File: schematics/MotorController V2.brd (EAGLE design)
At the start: 120.6 x 100 mm, 52 parts, among them IC1 7805, Q1 BC307

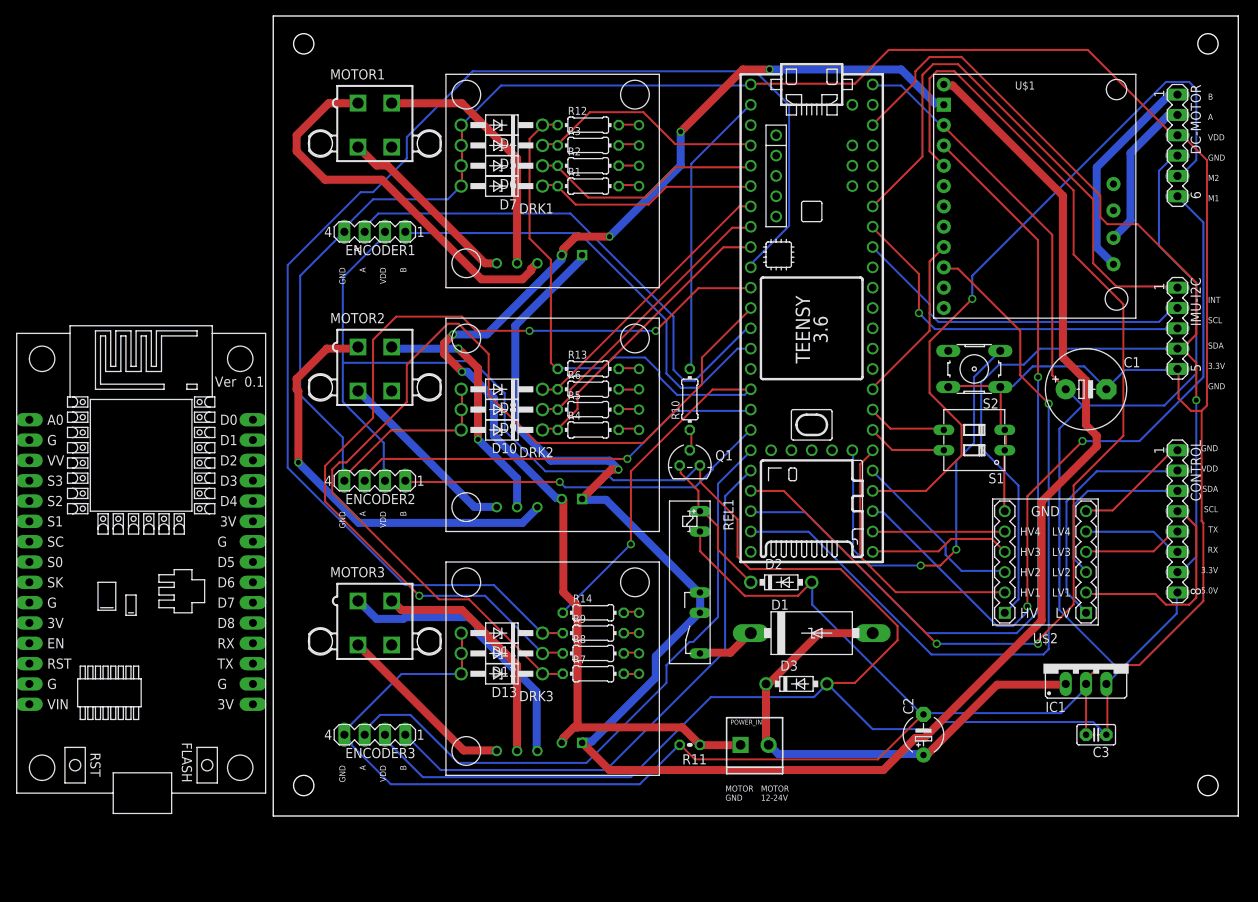
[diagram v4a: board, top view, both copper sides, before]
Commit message: i2c between webserver and bot controller
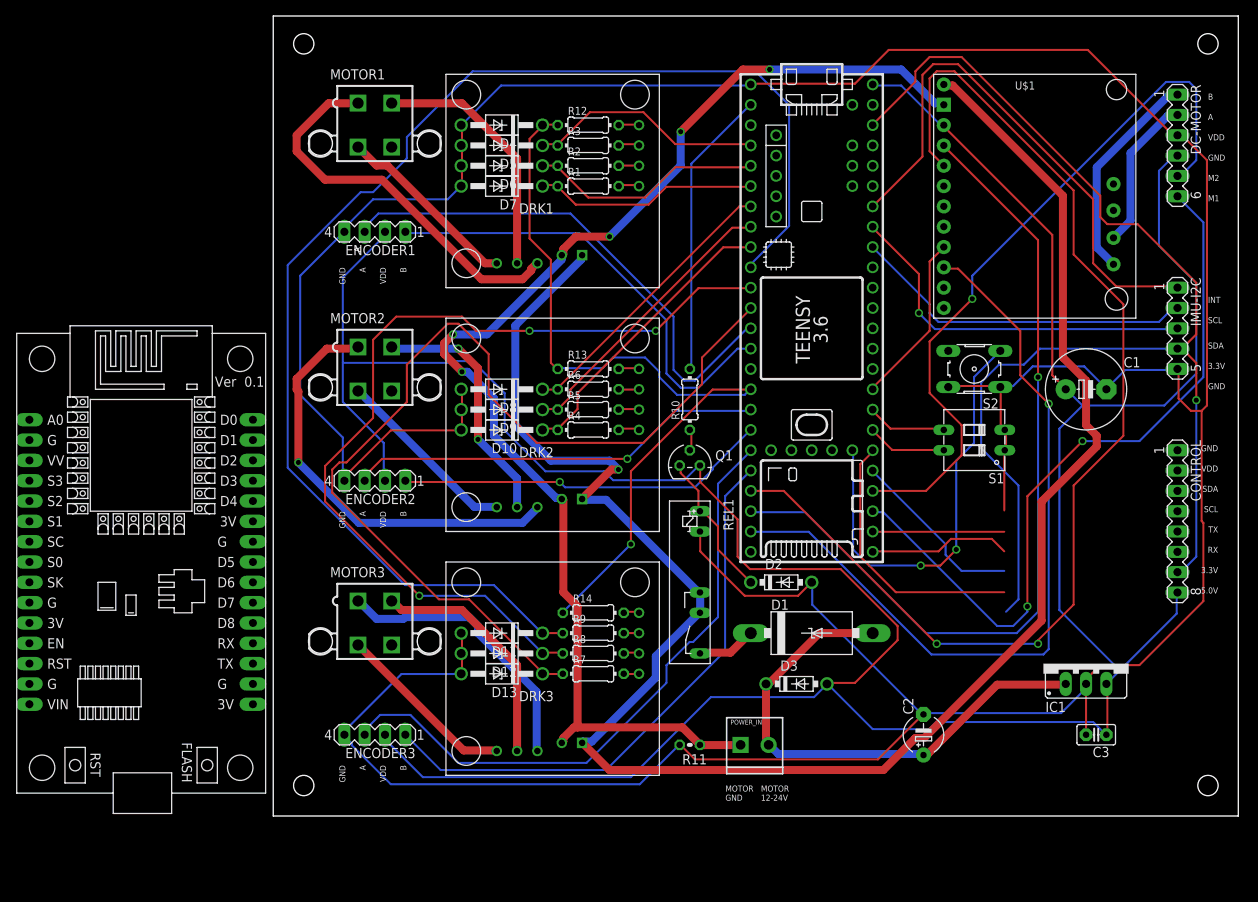
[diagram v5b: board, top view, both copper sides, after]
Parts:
- removed U$2: LEVEL-SHIFTER-4CHLEVEL-SHIFTER-4CH-ADAFRUIT, diy-modules:LEVEL-SHIFTER-4CH-ADAFRUIT
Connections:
- removed net CTR-SCL: CONTROL.4, U$2.LV1
- removed net CTR-SDA: CONTROL.3, U$2.LV2
- removed net CTRL-GND: CONTROL.1, U$2.GNDL
- removed net CTRL-RX: CONTROL.6, U$2.LV4
- removed net CTRL-TX: CONTROL.5, U$2.LV3
- removed net CTRL-VDD: CONTROL.2, U$2.LV
- net CTRL-3.3V: no longer U$2.HV
- net CTRL-5.0V: now also U$3.15
- net GND: no longer U$2.GNDH
- net RX5: no longer U$2.HV4
- net SCL1: now also U$3.28; no longer U$2.HV1
- net SDA1: now also U$3.29; no longer U$2.HV2
- net TX5: no longer U$2.HV3
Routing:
- net CTRL-VDD: track 30.4 -> 0.00 mm
- net CTR-SCL: track 26.9 -> 0.00 mm
- net CTR-SDA: track 22.7 -> 0.00 mm
- net CTRL-GND: track 14.7 -> 0.00 mm
- net CTRL-TX: track 12.5 -> 0.00 mm
- net CTRL-RX: track 12.5 -> 0.00 mm

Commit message: updated
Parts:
- added LED1: (no value), led:LED3MM
- added R15: 4,7K, resistor:0204/7
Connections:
- new net N$41: LED1.A, R15.2
- net CTRL-3.3V: now also CONTROL.2; no longer CONTROL.7
- net CTRL-5.0V: now also CONTROL.3; no longer CONTROL.8
- net GND: now also CONTROL.1, R15.1
- net LIPO-VDD: now also LED1.K
- net RX5: now also CONTROL.5
- net TX5: now also CONTROL.4, U$3.19
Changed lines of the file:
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@@
 </element>
 <element name="U$3" library="nodemcu" package="NODEMCU" value="NODEMCU" x="-91.44" y="17.78"/>
+<element name="LED1" library="led" library_urn="urn:adsk.eagle:library:259" package="LED3MM" package3d_urn="urn:adsk.eagle:package:15797/1" value="" x="-104.14" y="-16.51">
+<attribute name="NAME" x="-102.235" y="-16.129" size="1.27" layer="25" ratio="10"/>
+<attribute name="VALUE" x="-102.235" y="-18.161" size="1.27" layer="27" ratio="10"/>
+</element>
+<element name="R15" library="resistor" library_urn="urn:adsk.eagle:library:348" package="0204/7" package3d_urn="urn:adsk.eagle:package:23498/1" value="4,7K" x="-101.6" y="-21.59">
+<attribute name="NAME" x="-104.14" y="-20.2946" size="0.9906" layer="25" ratio="10"/>
+<attribute name="VALUE" x="-103.2256" y="-22.0726" size="0.9906" layer="27" ratio="10"/>
+</element>
 </elements>
 <signals>
@@
 <contactref element="ENCODER1" pad="2"/>
 <contactref element="D3" pad="A"/>
-<contactref element="CONTROL" pad="8"/>
 <wire x1="29.337" y1="-3.77825" x2="29.337" y2="2.44475" width="0.254" layer="1"/>
 <wire x1="29.337" y1="2.44475" x2="29.21" y2="2.54" width="0.254" layer="1"/>
@@
 <wire x1="29.337" y1="2.667" x2="30.89275" y2="4.22275" width="0.254" layer="16"/>
 <wire x1="30.89275" y1="4.22275" x2="38.00475" y2="11.33475" width="0.254" layer="16"/>
-<wire x1="38.00475" y1="13.7795" x2="38.1" y2="13.97" width="0.254" layer="16"/>
 <wire x1="29.337" y1="2.667" x2="29.21" y2="2.54" width="0.254" layer="16"/>
 <wire x1="3.556" y1="77.343" x2="0" y2="77.343" width="0.254" layer="16"/>
@@
 <wire x1="-5.55625" y1="2.44475" x2="-5.715" y2="2.54" width="0.254" layer="16"/>
 <contactref element="U$3" pad="15"/>
+<contactref element="CONTROL" pad="3"/>
 <wire x1="-60.96" y1="-3.81" x2="-105.41" y2="0" width="0" layer="19" extent="1-1"/>
+<wire x1="38.1" y1="26.67" x2="36.449" y2="37.338" width="0" layer="19" extent="16-16"/>
 </signal>
 <signal name="GND">
@@
 <contactref element="U$3" pad="14"/>
 <contactref element="U$3" pad="17"/>
+<contactref element="CONTROL" pad="1"/>
+<contactref element="R15" pad="1"/>
+<wire x1="-105.41" y1="2.54" x2="-105.41" y2="-21.59" width="0" layer="19" extent="1-1"/>
 <wire x1="-105.41" y1="12.7" x2="-105.41" y2="2.54" width="0" layer="19" extent="1-1"/>
 <wire x1="-105.41" y1="33.02" x2="-105.41" y2="12.7" width="0" layer="19" extent="1-1"/>
 <wire x1="-77.47" y1="2.54" x2="-105.41" y2="2.54" width="0" layer="19" extent="1-1"/>
 <wire x1="-66.00825" y1="-3.33375" x2="-77.47" y2="2.54" width="0" layer="19" extent="16-16"/>
+<wire x1="38.1" y1="31.75" x2="39.78275" y2="36.67125" width="0" layer="19" extent="1-1"/>
 <wire x1="-77.47" y1="20.32" x2="-66.2305" y2="28.0035" width="0" layer="19" extent="16-16"/>
 </signal>
@@
 <wire x1="-36.22675" y1="-4.8895" x2="-36.322" y2="-4.826" width="1" layer="1"/>
 <via x="-31.78175" y="29.337" extent="1-16" drill="0.635"/>
+<contactref element="LED1" pad="K"/>
+<wire x1="-36.322" y1="-4.826" x2="-102.87" y2="-16.51" width="0" layer="19" extent="1-1"/>
 </signal>
 <signal name="N$13" class="1">
@@
 <contactref element="PRJ1" pad="3V3_LO"/>
 <contactref element="IMU-I2C" pad="4"/>
-<contactref element="CONTROL" pad="7"/>
 <wire x1="5.334" y1="77.7875" x2="0" y2="72.4535" width="0.254" layer="1"/>
 <wire x1="5.334" y1="79.121" x2="5.334" y2="77.7875" width="0.254" layer="1"/>
@@
 <wire x1="40.4495" y1="42.672" x2="40.4495" y2="38.00475" width="0.254" layer="1"/>
 <wire x1="38.6715" y1="44.45" x2="40.4495" y2="42.672" width="0.254" layer="1"/>
-<wire x1="38.227" y1="16.66875" x2="38.1" y2="16.51" width="0.254" layer="16"/>
 <wire x1="38.6715" y1="44.45" x2="38.1" y2="44.45" width="0.254" layer="1"/>
 <via x="40.4495" y="38.00475" extent="1-16" drill="0.635"/>
+<contactref element="CONTROL" pad="2"/>
+<wire x1="40.4495" y1="38.00475" x2="38.1" y2="29.21" width="0" layer="19" extent="16-16"/>
 </signal>
 <signal name="IMU-INT">
@@
 <wire x1="16.4465" y1="21.55825" x2="0" y2="21.55825" width="0.254" layer="1"/>
 <wire x1="0" y1="21.55825" x2="0" y2="21.59" width="0.254" layer="1"/>
+<contactref element="CONTROL" pad="5"/>
+<wire x1="16.4465" y1="21.55825" x2="38.1" y2="21.59" width="0" layer="19" extent="1-1"/>
 </signal>
 <signal name="TX5">
@@
 <wire x1="16.4465" y1="19.1135" x2="14.89075" y2="20.66925" width="0.254" layer="1"/>
 <wire x1="0" y1="19.1135" x2="0" y2="19.05" width="0.254" layer="1"/>
+<contactref element="U$3" pad="19"/>
+<contactref element="CONTROL" pad="4"/>
+<wire x1="0" y1="19.05" x2="-77.47" y2="7.62" width="0" layer="19" extent="1-1"/>
+<wire x1="38.1" y1="24.13" x2="16.4465" y2="19.1135" width="0" layer="19" extent="1-1"/>
 </signal>
 <signal name="IMU-SCL">
@@
 <wire x1="-77.47" y1="22.86" x2="-77.47" y2="0" width="0" layer="19" extent="1-1"/>
 </signal>
+<signal name="N$41">
+<contactref element="R15" pad="2"/>
+<contactref element="LED1" pad="A"/>
+<wire x1="-97.79" y1="-21.59" x2="-105.41" y2="-16.51" width="0" layer="19" extent="1-1"/>
+</signal>
 </signals>

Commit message: no message
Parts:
- C1: device rcl:E5-10,5 -> rcl:E2,5-6
- LED1: value (none) -> red
- moved U$3 112.5 mm to (15.2, 53.3), turned to 180 degrees
- moved LED1 84.8 mm to (-20.3, -3.81)
- moved R15 79.2 mm to (-24.1, -5.08), turned to 90 degrees
- moved U$1 57.5 mm to (19.1, 7.62)
- moved C1 38.1 mm to (7.62, 6.35), turned to 90 degrees
- moved S2 37.8 mm to (0.00, 6.35)
- moved R10 29.0 mm to (-11.4, 11.4), turned to 0 degrees
- moved C3 28.1 mm to (0.00, -6.35), turned to 90 degrees
- moved IC1 23.3 mm to (5.08, -3.81), turned to 90 degrees
- moved Q1 17.8 mm to (-22.9, 12.1), turned to 180 degrees
- moved S1 17.7 mm to (6.35, 16.5), turned to 270 degrees
- moved D2 16.6 mm to (-20.3, 1.27)
- moved C2 13.0 mm to (-6.35, -6.35), turned to 270 degrees
- moved CONTROL 12.7 mm to (38.1, 35.6)
- moved REL1 10.2 mm to (-11.4, 16.5), turned to 180 degrees
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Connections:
- net CTRL-3.3V renamed 3.3V
- new net N$49: CONTROL.8, U$3.30
- new net N$50: CONTROL.7, U$3.13
- new net N$51: CONTROL.6, PRJ1.14/A0
- net SCL1: now also U$3.29; no longer U$3.28
- net SDA1: now also U$3.28; no longer U$3.29
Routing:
- net N$51: track 0.00 -> 105.1 mm, vias 0 -> 1
- net N$60: track 21.5 -> 118.4 mm
- net N$28: track 111.7 -> 208.2 mm, vias 3 -> 0
- net N$44: track 143.7 -> 49.7 mm, vias 2 -> 1
- net N$12: track 10.1 -> 100.5 mm
- net TX5: track 17.8 -> 103.9 mm
- net 3.3V: track 155.4 -> 81.2 mm
- net N$27: track 166.6 -> 100.0 mm, vias 0 -> 1
- net LIPO-VDD: track 236.1 -> 171.2 mm, vias 1 -> 3
- net N$47: track 106.5 -> 43.5 mm, vias 1 -> 0
- net CTRL-5.0V: track 399.0 -> 337.3 mm, vias 0 -> 2
- net BLCK-M2: track 19.3 -> 79.6 mm
- net 3V: track 0.00 -> 58.7 mm
- net RED-M1: track 26.9 -> 84.8 mm
- net IMU-SDA: track 46.4 -> 100.3 mm
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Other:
- board text removed: "5.0V"
- board text removed: "RX"
- board text removed: "TX"

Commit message: board now with ESP8266
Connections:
- net CTRL-5.0V renamed +5V
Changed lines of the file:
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@@
 </elements>
 <signals>
-<signal name="CTRL-5.0V">
+<signal name="+5V">
 <contactref element="PRJ1" pad="VIN"/>
 <contactref element="C1" pad="+"/>
